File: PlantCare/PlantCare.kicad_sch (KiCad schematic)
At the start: 8 parts, among them J1 USB4105-GF-A

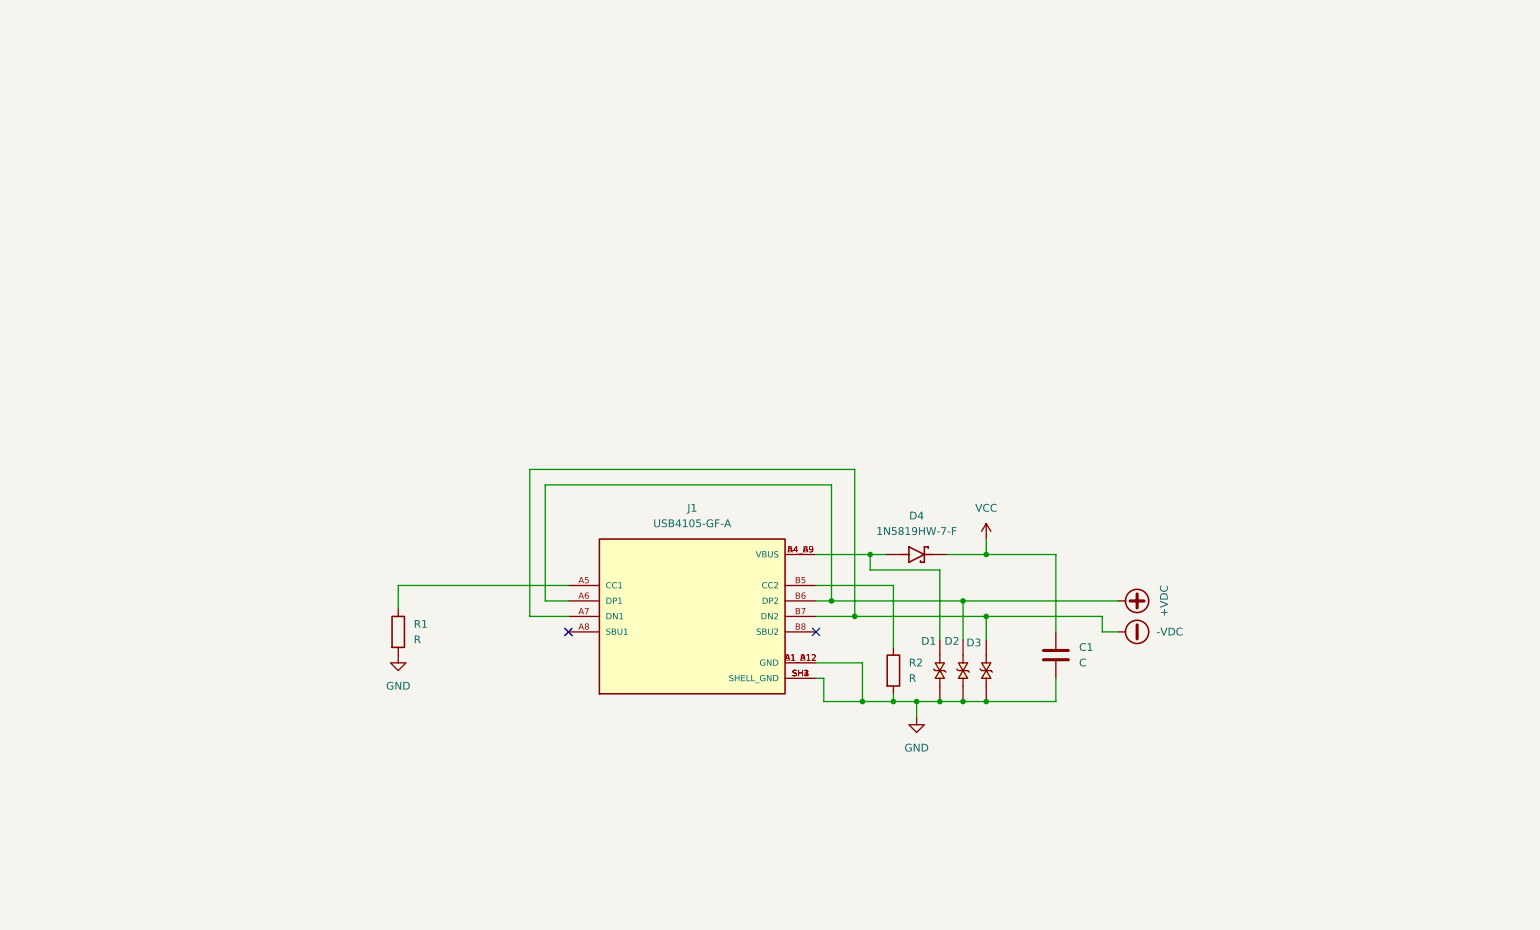
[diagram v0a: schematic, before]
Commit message: Add voltage regulator
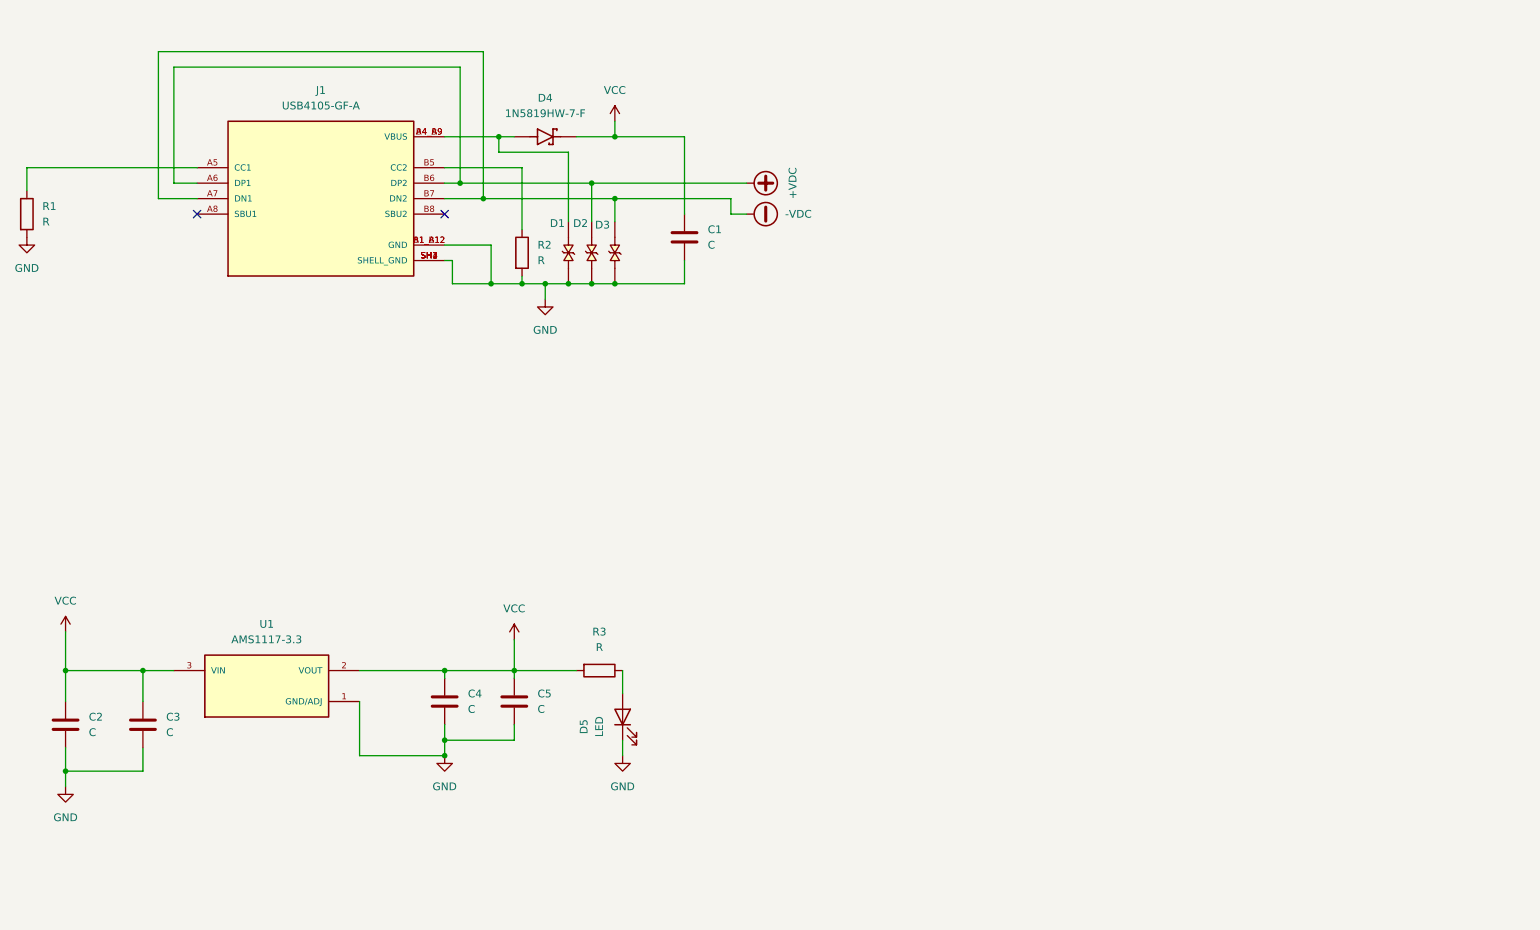
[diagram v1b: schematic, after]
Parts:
- added C2, C3, C4, C5: C, symbol Device:C
- added D5: LED, symbol Device:LED
- added R3: R, symbol Device:R
- added U1: AMS1117-3.3, SOT229P700X180-4N, symbol AMS1117-3.3:AMS1117-3.3
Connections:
- net GND: now also C2.2, C3.2, C4.2, C5.2, D5.1 (K), U1.1 (GND/ADJ)
- net VCC: now also C2.1, C3.1, C4.1, C5.1, R3.2, U1.2 (VOUT), U1.3 (VIN)
- new net: D5.2 (A), R3.1
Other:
- moved on the sheet: C1, D1, D2, D3, D4, J1, R1, R2

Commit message: Add rgb led
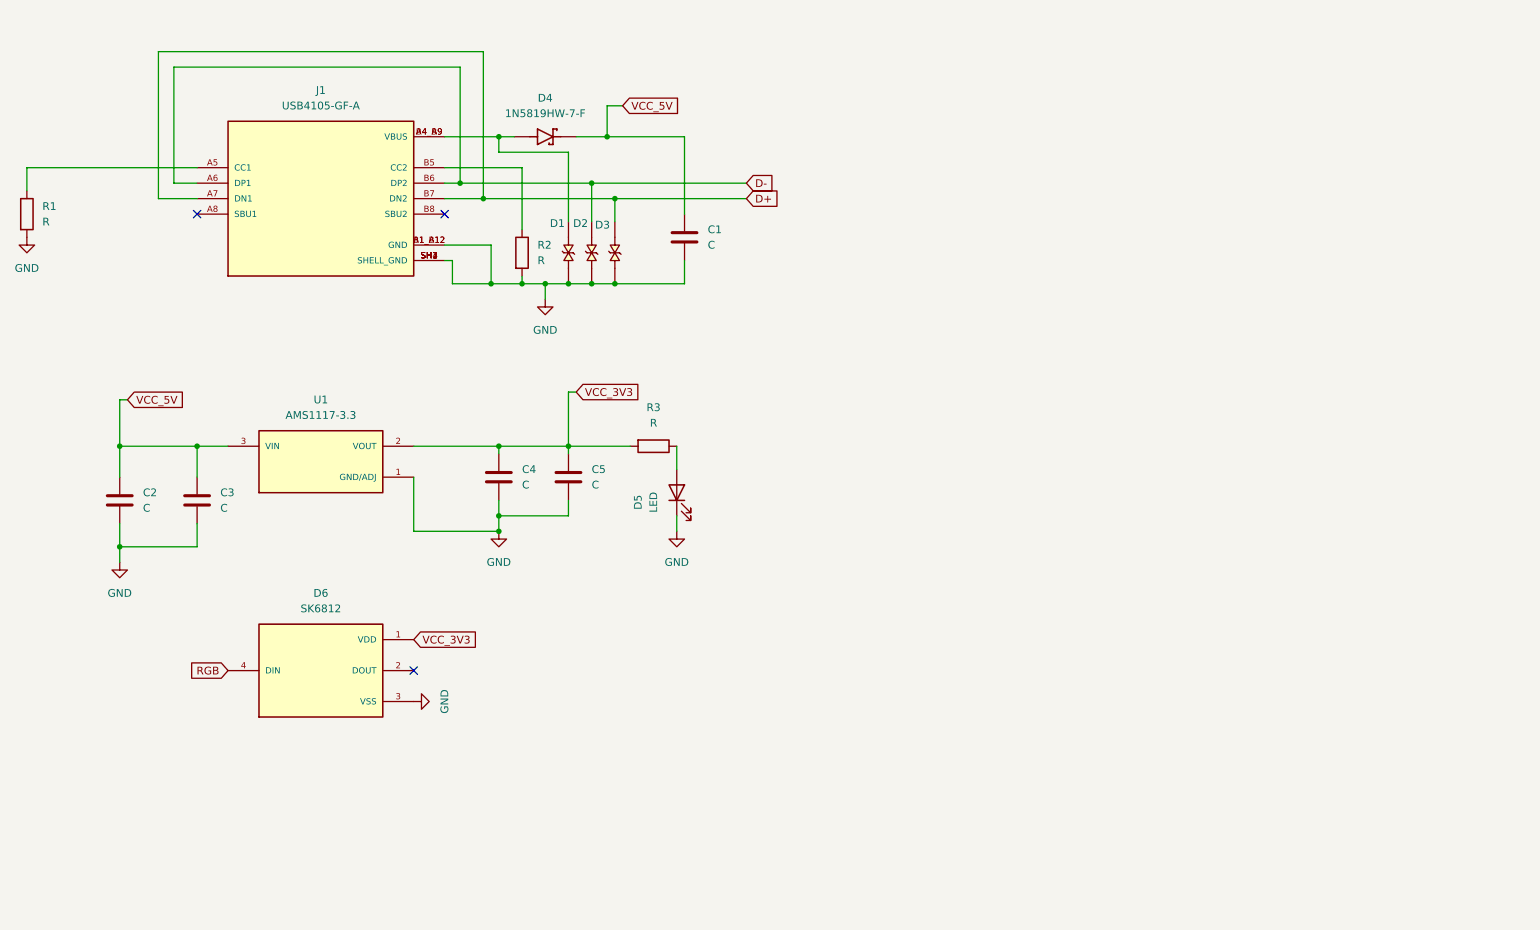
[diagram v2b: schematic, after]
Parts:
- added D6: SK6812, LED_SK6812, symbol SK6812:SK6812
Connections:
- net GND: now also D6.3 (VSS)
- net +VDC renamed D-
- net -VDC renamed D+
- net VCC renamed VCC_5V
- net VCC_5V: no longer C4.1, C5.1, R3.2, U1.2 (VOUT)
- new net RGB: D6.4 (DIN)
- new net VCC_3V3: C4.1, C5.1, D6.1 (VDD), R3.2, U1.2 (VOUT)
- no-connect marks 2 -> 3
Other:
- moved on the sheet: C2, C3, C4, C5, D5, R3, U1

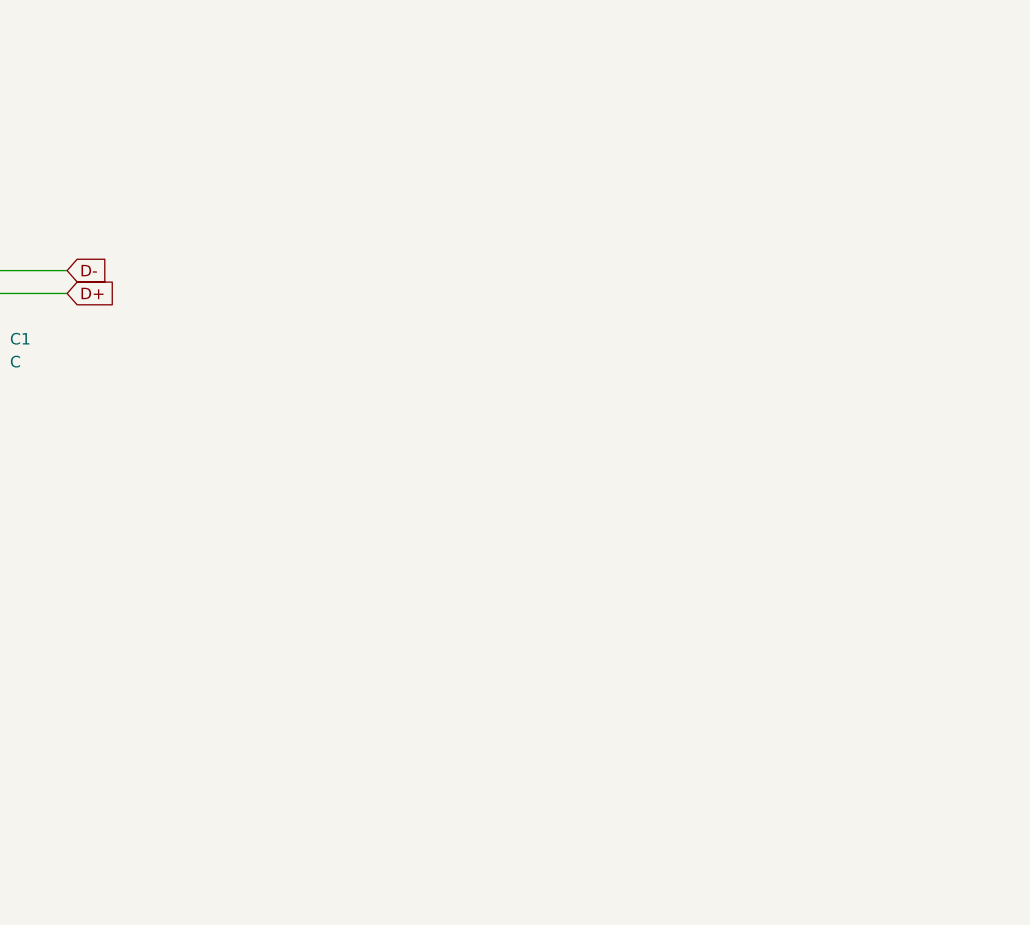
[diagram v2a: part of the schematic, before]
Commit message: Add esp32-s3-1-n16r2 scheme
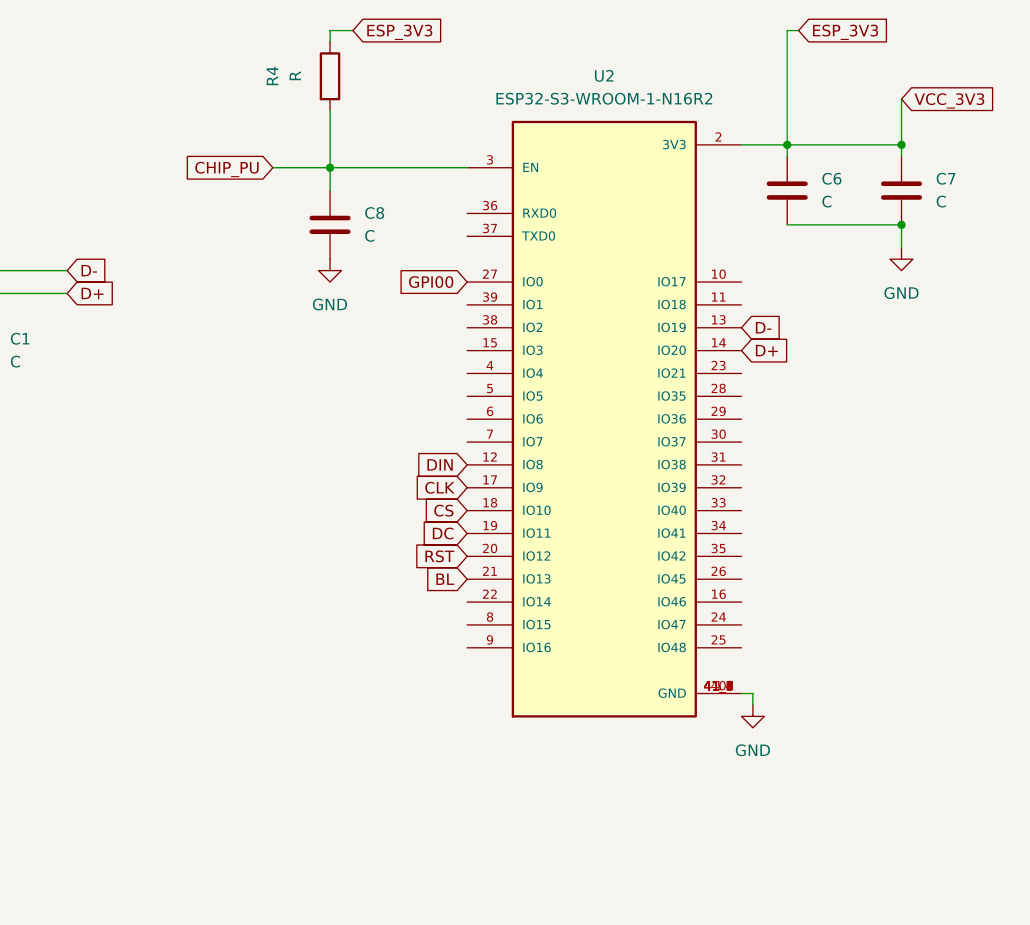
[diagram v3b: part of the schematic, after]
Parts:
- added C6, C7, C8: C, symbol Device:C
- added R4: R, symbol Device:R
- added U2: ESP32-S3-WROOM-1-N16R2, XCVR_ESP32-S3-WROOM-1-N16R2, symbol ESP32-S3-WROOM-1-N16R2:ESP32-S3-WROOM-1-N16R2
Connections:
- net D+: now also U2.14 (IO20)
- net D-: now also U2.13 (IO19)
- net GND: now also C6.2, C7.2, C8.2, U2.1 (GND), U2.40 (GND), U2.41_1 (GND), U2.41_2 (GND), U2.41_3 (GND), U2.41_4 (GND), U2.41_5 (GND), U2.41_6 (GND), U2.41_7 (GND), U2.41_8 (GND), U2.41_9 (GND)
- net VCC_3V3 renamed ESP_3V3
- net ESP_3V3: now also C6.1, C7.1, R4.1, U2.2 (3V3)
- new net BL: U2.21 (IO13)
- new net CHIP_PU: C8.1, R4.2, U2.3 (EN)
- new net CLK: U2.17 (IO9)
- new net CS: U2.18 (IO10)
- new net DC: U2.19 (IO11)
- new net DIN: U2.12 (IO8)
- new net GPI00: U2.27 (IO0)
- new net RST: U2.20 (IO12)

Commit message: Add complete schemes
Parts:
- added C10, C9: C, symbol Device:C
- added R5, R6: R, symbol Device:R
- added SW1, SW2: PTS810_SJM_250_SMTR_LFS, SW_PTS810_SJM_250_SMTR_LFS, symbol PTS810_SJM_250_SMTR_LFS:PTS810_SJM_250_SMTR_LFS
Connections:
- net CHIP_PU: now also C10.1, R6.2, SW2.3
- net ESP_3V3: now also R5.1, R6.1
- net GND: now also C10.2, C9.2, SW1.2, SW2.2
- new net: C9.1, R5.2, SW1.3
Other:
- note added: "Buttons"
- note added: "ESP32-S3-WROOM"
- note added: "RGB LED"
- note added: "S3 Display"
- note added: "USB-C"
- note added: "Voltage Regulator"
- title: (none) -> PLANTCARE MOISTURE MODULE SCHEME
- moved on the sheet: C1, C2, C3, C4, C5, C6, C7, C8, D1, D2, D3, D4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

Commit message: Link footprints
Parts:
- C1, C10, C2, C3, C4, C5, C6, C7, C8, C9: footprint (none) -> Capacitor_Tantalum_SMD:CP_EIA-1608-08_AVX-J
- D1, D2, D3: footprint TVS_LESD5D5.0CT1G -> LESD5D5.0CT1G-footprint:TVS_LESD5D5.0CT1G
- D4: footprint SOD3715X145N -> 1N5819HW-7-F-footprint:SOD3715X145N
- D5: footprint (none) -> Diode_SMD:D_0805_2012Metric
- D6: footprint LED_SK6812 -> SK6812-footprint:LED_SK6812
- J1: footprint GCT_USB4105-GF-A -> USB4105-GF-A-footprint:GCT_USB4105-GF-A
- R1, R2, R3, R4, R5, R6: footprint (none) -> Resistor_SMD:R_0201_0603Metric
- SW1, SW2: footprint SW_PTS810_SJM_250_SMTR_LFS -> PTS810_SJM_250_SMTR_LFS-footprint:SW_PTS810_SJM_250_SMTR_LFS
- U1: footprint SOT229P700X180-4N -> AMS1117-3.3-footprint:SOT229P700X180-4N
- U2: footprint XCVR_ESP32-S3-WROOM-1-N16R2 -> ESP32-S3-WROOM-1-N16R2-footprint:XCVR_ESP32-S3-WROOM-1-N16R2
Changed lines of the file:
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@@
 			)
 		)
-		(property "Footprint" ""
+		(property "Footprint" "Resistor_SMD:R_0201_0603Metric"
 			(at 21.082 48.26 90)
 			(effects
@@
 			)
 		)
-		(property "Footprint" ""
+		(property "Footprint" "Resistor_SMD:R_0201_0603Metric"
 			(at 125.73 85.852 90)
 			(effects
@@
 			)
 		)
-		(property "Footprint" ""
+		(property "Footprint" "Capacitor_Tantalum_SMD:CP_EIA-1608-08_AVX-J"
 			(at 51.7652 100.33 0)
 			(effects
@@
 			)
 		)
-		(property "Footprint" ""
+		(property "Footprint" "Resistor_SMD:R_0201_0603Metric"
 			(at 183.642 34.29 90)
 			(effects
@@
 			)
 		)
-		(property "Footprint" ""
+		(property "Footprint" "Capacitor_Tantalum_SMD:CP_EIA-1608-08_AVX-J"
 			(at 112.7252 96.52 0)
 			(effects
@@
 			)
 		)
-		(property "Footprint" "TVS_LESD5D5.0CT1G"
+		(property "Footprint" "LESD5D5.0CT1G-footprint:TVS_LESD5D5.0CT1G"
 			(at 115.57 54.61 0)
 			(effects
@@
 			)
 		)
-		(property "Footprint" "SW_PTS810_SJM_250_SMTR_LFS"
+		(property "Footprint" "PTS810_SJM_250_SMTR_LFS-footprint:SW_PTS810_SJM_250_SMTR_LFS"
 			(at 81.28 139.7 0)
 			(effects
@@
 			)
 		)
-		(property "Footprint" ""
+		(property "Footprint" "Capacitor_Tantalum_SMD:CP_EIA-1608-08_AVX-J"
 			(at 186.3852 54.61 0)
 			(effects
@@
 			)
 		)
-		(property "Footprint" ""
+		(property "Footprint" "Diode_SMD:D_0805_2012Metric"
 			(at 129.54 95.25 0)
 			(effects
@@
 			)
 		)
-		(property "Footprint" ""
+		(property "Footprint" "Capacitor_Tantalum_SMD:CP_EIA-1608-08_AVX-J"
 			(at 249.8852 50.8 0)
 			(effects
@@
 			)
 		)
-		(property "Footprint" "LED_SK6812"
+		(property "Footprint" "SK6812-footprint:LED_SK6812"
 			(at 236.22 139.7 0)
 			(effects
@@
 			)
 		)
-		(property "Footprint" "TVS_LESD5D5.0CT1G"
+		(property "Footprint" "LESD5D5.0CT1G-footprint:TVS_LESD5D5.0CT1G"
 			(at 111.76 54.61 0)
 			(effects
@@
 			)
 		)
-		(property "Footprint" ""
+		(property "Footprint" "Resistor_SMD:R_0201_0603Metric"
 			(at 98.552 138.43 90)
 			(effects
@@
 			)
 		)
-		(property "Footprint" ""
+		(property "Footprint" "Capacitor_Tantalum_SMD:CP_EIA-1608-08_AVX-J"
 			(at 54.3052 152.4 0)
 			(effects
@@
 			)
 		)
-		(property "Footprint" "SOD3715X145N"
+		(property "Footprint" "1N5819HW-7-F-footprint:SOD3715X145N"
 			(at 107.95 35.56 0)
 			(effects
@@
 			)
 		)
-		(property "Footprint" "SOT229P700X180-4N"
+		(property "Footprint" "AMS1117-3.3-footprint:SOT229P700X180-4N"
 			(at 71.12 90.17 0)
 			(effects
@@
 			)
 		)
-		(property "Footprint" ""
+		(property "Footprint" "Capacitor_Tantalum_SMD:CP_EIA-1608-08_AVX-J"
 			(at 131.7752 55.88 0)
 			(effects
@@
 			)
 		)
-		(property "Footprint" ""
+		(property "Footprint" "Capacitor_Tantalum_SMD:CP_EIA-1608-08_AVX-J"
 			(at 96.2152 151.13 0)
 			(effects
@@
 			)
 		)
-		(property "Footprint" ""
+		(property "Footprint" "Capacitor_Tantalum_SMD:CP_EIA-1608-08_AVX-J"
 			(at 237.1852 50.8 0)
 			(effects
@@
 			)
 		)
-		(property "Footprint" "GCT_USB4105-GF-A"
+		(property "Footprint" "USB4105-GF-A-footprint:GCT_USB4105-GF-A"
 			(at 71.12 45.72 0)
 			(effects
@@
 			)
 		)
-		(property "Footprint" ""
+		(property "Footprint" "Resistor_SMD:R_0201_0603Metric"
 			(at 54.102 135.89 90)
 			(effects
@@
 			)
 		)
-		(property "Footprint" "XCVR_ESP32-S3-WROOM-1-N16R2"
+		(property "Footprint" "ESP32-S3-WROOM-1-N16R2-footprint:XCVR_ESP32-S3-WROOM-1-N16R2"
 			(at 215.9 72.39 0)
 			(effects
@@
 			)
 		)
-		(property "Footprint" "SW_PTS810_SJM_250_SMTR_LFS"
+		(property "Footprint" "PTS810_SJM_250_SMTR_LFS-footprint:SW_PTS810_SJM_250_SMTR_LFS"
 			(at 39.37 140.97 0)
 			(effects
@@
 			)
 		)
-		(property "Footprint" ""
+		(property "Footprint" "Capacitor_Tantalum_SMD:CP_EIA-1608-08_AVX-J"
 			(at 101.2952 96.52 0)
 			(effects
@@
 			)
 		)
-		(property "Footprint" ""
+		(property "Footprint" "Capacitor_Tantalum_SMD:CP_EIA-1608-08_AVX-J"
 			(at 39.0652 100.33 0)
 			(effects
@@
 			)
 		)
-		(property "Footprint" ""
+		(property "Footprint" "Resistor_SMD:R_0201_0603Metric"
 			(at 102.362 54.61 90)
 			(effects
@@
 			)
 		)
-		(property "Footprint" "TVS_LESD5D5.0CT1G"
+		(property "Footprint" "LESD5D5.0CT1G-footprint:TVS_LESD5D5.0CT1G"
 			(at 119.38 54.61 0)
 			(effects

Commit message: Clean scheme
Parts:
- removed C1, C10, C2, C3, C4, C5, C6, C7, C8, C9: C, Capacitor_Tantalum_SMD:CP_EIA-1608-08_AVX-J, symbol Device:C
- removed D1, D2, D3: ~, LESD5D5.0CT1G-footprint:TVS_LESD5D5.0CT1G, symbol LESD5D5.0CT1G:LESD5D5.0CT1G
- removed D4: 1N5819HW-7-F, 1N5819HW-7-F-footprint:SOD3715X145N, symbol 1N5819HW-7-F:1N5819HW-7-F
- removed D5: LED, Diode_SMD:D_0805_2012Metric, symbol Device:LED
- removed D6: SK6812, SK6812-footprint:LED_SK6812, symbol SK6812:SK6812
- removed J1: USB4105-GF-A, USB4105-GF-A-footprint:GCT_USB4105-GF-A, symbol USB4105-GF-A:USB4105-GF-A
- removed R1, R2, R3, R4, R5, R6: R, Resistor_SMD:R_0201_0603Metric, symbol Device:R
- removed SW1, SW2: PTS810_SJM_250_SMTR_LFS, PTS810_SJM_250_SMTR_LFS-footprint:SW_PTS810_SJM_250_SMTR_LFS, symbol PTS810_SJM_250_SMTR_LFS:PTS810_SJM_250_SMTR_LFS
- removed U1: AMS1117-3.3, AMS1117-3.3-footprint:SOT229P700X180-4N, symbol AMS1117-3.3:AMS1117-3.3
- removed U2: ESP32-S3-WROOM-1-N16R2, ESP32-S3-WROOM-1-N16R2-footprint:XCVR_ESP32-S3-WROOM-1-N16R2, symbol ESP32-S3-WROOM-1-N16R2:ESP32-S3-WROOM-1-N16R2
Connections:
- no-connect marks 3 -> 0
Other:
- note removed: "Buttons"
- note removed: "ESP32-S3-WROOM"
- note removed: "RGB LED"
- note removed: "S3 Display"
- note removed: "USB-C"
- note removed: "Voltage Regulator"

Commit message: Add power supply scheme
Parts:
- added C1, C2: C, symbol Device:C
- added R1: R_US, symbol Device:R_US
- added U1: AMS1117-3.3, SOT229P700X180-4N, symbol AMS1117-3.3:AMS1117-3.3
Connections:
- new net: C2.1, U1.2 (VOUT)
- new net: C1.1, R1.1, U1.3 (VIN)
- new net GND: C1.2, C2.2, R1.2, U1.1 (GND/ADJ)
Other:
- note added: "POWER SUPPLY"
